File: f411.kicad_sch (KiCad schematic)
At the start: 19 parts, among them J18 Conn_02x04_Top_Bottom, SW1 SW_Push, SW2 SW_Push, U5 STM32F411CEU6

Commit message: completed cleanup of v0.2.0 fixes and switch radio side.
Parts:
- J18: Manufacturer (none) -> Hong Cheng; MfgPart (none) -> HC-PM254-5.0H-2x8PS; Notes (none) -> or equivalent
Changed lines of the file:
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@@
 			)
 		)
+		(property "Note" ""
+			(at 64.77 63.5 0)
+			(effects
+				(font
+					(size 1.27 1.27)
+				)
+				(hide yes)
+			)
+		)
 		(pin "2"
 		)
@@
 			)
 		)
+		(property "Note" ""
+			(at 186.69 152.4 90)
+			(effects
+				(font
+					(size 1.27 1.27)
+				)
+				(hide yes)
+			)
+		)
 		(pin "1"
 		)
@@
 			)
 		)
+		(property "Note" ""
+			(at 167.64 87.63 0)
+			(effects
+				(font
+					(size 1.27 1.27)
+				)
+				(hide yes)
+			)
+		)
 		(pin "1"
 		)
@@
 			)
 		)
+		(property "Note" ""
+			(at 123.19 139.7 0)
+			(effects
+				(font
+					(size 1.27 1.27)
+				)
+				(hide yes)
+			)
+		)
 		(pin "1"
 		)
@@
 			)
 		)
+		(property "Note" ""
+			(at 69.85 85.09 0)
+			(effects
+				(font
+					(size 1.27 1.27)
+				)
+				(hide yes)
+			)
+		)
 		(pin "1"
 		)
@@
 			)
 		)
+		(property "Note" ""
+			(at 106.68 100.33 0)
+			(effects
+				(font
+					(size 1.27 1.27)
+				)
+				(hide yes)
+			)
+		)
 		(pin "1"
 		)
@@
 			)
 		)
+		(property "Note" ""
+			(at 96.52 109.22 0)
+			(effects
+				(font
+					(size 1.27 1.27)
+				)
+				(hide yes)
+			)
+		)
 		(pin "1"
 		)
@@
 			)
 		)
-		(property "Datasheet" "~"
+		(property "Datasheet" "https://www.lcsc.com/datasheet/C42163136.pdf"
 			(at 175.26 128.27 0)
 			(effects
@@
 			)
 		)
+		(property "Manufacturer" "Hong Cheng"
+			(at 175.26 128.27 0)
+			(effects
+				(font
+					(size 1.27 1.27)
+				)
+				(hide yes)
+			)
+		)
+		(property "MfgPart" "HC-PM254-5.0H-2x8PS"
+			(at 175.26 128.27 0)
+			(effects
+				(font
+					(size 1.27 1.27)
+				)
+				(hide yes)
+			)
+		)
+		(property "Note" ""
+			(at 175.26 128.27 0)
+			(effects
+				(font
+					(size 1.27 1.27)
+				)
+				(hide yes)
+			)
+		)
+		(property "Notes" "or equivalent"
+			(at 175.26 128.27 0)
+			(effects
+				(font
+					(size 1.27 1.27)
+				)
+				(hide yes)
+			)
+		)
 		(pin "a1"
 		)
@@
 			)
 		)
+		(property "Note" ""
+			(at 67.31 44.45 90)
+			(effects
+				(font
+					(size 1.27 1.27)
+				)
+				(hide yes)
+			)
+		)
 		(pin "1"
 		)
@@
 			)
 		)
+		(property "Note" ""
+			(at 58.42 59.69 0)
+			(effects
+				(font
+					(size 1.27 1.27)
+				)
+				(hide yes)
+			)
+		)
 		(pin "1"
 		)
@@
 			)
 		)
+		(property "Note" ""
+			(at 170.18 50.8 0)
+			(effects
+				(font
+					(size 1.27 1.27)
+				)
+				(hide yes)
+			)
+		)
 		(pin "1"
 		)
@@
 			)
 		)
+		(property "Note" ""
+			(at 71.12 39.37 0)
+			(effects
+				(font
+					(size 1.27 1.27)
+				)
+				(hide yes)
+			)
+		)
 		(pin "1"
 		)
@@
 			)
 		)
+		(property "Note" ""
+			(at 144.78 102.87 0)
+			(effects
+				(font
+					(size 1.27 1.27)
+				)
+				(hide yes)
+			)
+		)
 		(pin "49"
 		)
@@
 			)
 		)
+		(property "Note" ""
+			(at 170.18 43.18 0)
+			(effects
+				(font
+					(size 1.27 1.27)
+				)
+				(hide yes)
+			)
+		)
 		(pin "2"
 		)
@@
 			)
 		)
+		(property "Note" ""
+			(at 41.91 72.39 90)
+			(effects
+				(font
+					(size 1.27 1.27)
+				)
+				(hide yes)
+			)
+		)
 		(pin "1"
 		)
@@
 			)
 		)
+		(property "Note" ""
+			(at 93.98 40.64 0)
+			(effects
+				(font
+					(size 1.27 1.27)
+				)
+				(hide yes)
+			)
+		)
 		(pin "2"
 		)
@@
 			)
 		)
+		(property "Note" ""
+			(at 190.5 140.97 0)
+			(effects
+				(font
+					(size 1.27 1.27)
+				)
+				(hide yes)
+			)
+		)
 		(pin "1"
 		)
@@
 			)
 		)
+		(property "Note" ""
+			(at 62.23 85.09 90)
+			(effects
+				(font
+					(size 1.27 1.27)
+				)
+				(hide yes)
+			)
+		)
 		(pin "1"
 		)
@@
 			(at 41.91 80.01 0)
 			(effects
+				(font
+					(size 1.27 1.27)
+				)
+				(hide yes)
+			)
+		)
+		(property "Note" ""
+			(at 41.91 80.01 0)
+			(effects

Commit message: converted R, C, and L to smaller 0402 footprints. Some trace rearranging and cleanup.
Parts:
- C14: footprint ProjectLib:C_0603_1608Metric -> ProjectLib:C_0402_1005Metric; Manufacturer Samsung -> (none); MfgPart CL10A475KP8NNNC -> (none); Package C_0603_1608Metric -> C_0402_1005Metric
- C17, C9: footprint ProjectLib:C_0603_1608Metric -> ProjectLib:C_0402_1005Metric; Manufacturer Samsung -> (none); MfgPart CL10B104KB8NNNC -> (none); Package C_0603_1608Metric -> C_0402_1005Metric
- L1: footprint ProjectLib:L_TDK_MLZ1608 -> ProjectLib:L_0402_1005Metric; MfgPart MLZ1608N2R2LT000 -> MLZ1005M2R2WT000; Package L_0603_1608Metric -> L_0402_1005Metric
- R23, R24: footprint ProjectLib:R_0603_1608Metric -> ProjectLib:R_0402_1005Metric; Package R_0603_1608Metric -> R_0402_1005Metric
- R25, R26, R27, R33, R34: footprint ProjectLib:R_0603_1608Metric -> ProjectLib:R_0402_1005Metric; Manufacturer Vishay -> (none); MfgPart CRCW060310K0FKEA -> (none); Package R_0603_1608Metric -> R_0402_1005Metric
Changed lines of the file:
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@@
 			)
 		)
-		(property "Footprint" "ProjectLib:R_0603_1608Metric"
+		(property "Footprint" "ProjectLib:R_0402_1005Metric"
 			(at 62.992 63.5 90)
 			(effects
@@
 			)
 		)
-		(property "Manufacturer" "Vishay"
+		(property "Manufacturer" ""
 			(at 64.77 63.5 0)
 			(effects
@@
 			)
 		)
-		(property "MfgPart" "CRCW060310K0FKEA"
+		(property "MfgPart" ""
 			(at 64.77 63.5 0)
 			(effects
@@
 			)
 		)
-		(property "Package" "R_0603_1608Metric"
+		(property "Package" "R_0402_1005Metric"
 			(at 64.77 63.5 0)
 			(effects
@@
 			)
 		)
-		(property "Footprint" "ProjectLib:R_0603_1608Metric"
+		(property "Footprint" "ProjectLib:R_0402_1005Metric"
 			(at 185.674 152.654 90)
 			(effects
@@
 			)
 		)
-		(property "Manufacturer" "Vishay"
+		(property "Manufacturer" ""
 			(at 186.69 152.4 0)
 			(effects
@@
 			)
 		)
-		(property "MfgPart" "CRCW060310K0FKEA"
+		(property "MfgPart" ""
 			(at 186.69 152.4 0)
 			(effects
@@
 			)
 		)
-		(property "Package" "R_0603_1608Metric"
+		(property "Package" "R_0402_1005Metric"
 			(at 186.69 152.4 0)
 			(effects
@@
 			)
 		)
-		(property "Footprint" "ProjectLib:C_0603_1608Metric"
+		(property "Footprint" "ProjectLib:C_0402_1005Metric"
 			(at 124.1552 143.51 0)
 			(effects
@@
 			)
 		)
-		(property "Manufacturer" "Samsung"
+		(property "Manufacturer" ""
 			(at 123.19 139.7 0)
 			(effects
@@
 			)
 		)
-		(property "MfgPart" "CL10A475KP8NNNC"
+		(property "MfgPart" ""
 			(at 123.19 139.7 0)
 			(effects
@@
 			)
 		)
-		(property "Package" "C_0603_1608Metric"
+		(property "Package" "C_0402_1005Metric"
 			(at 123.19 139.7 0)
 			(effects
@@
 			)
 		)
-		(property "Footprint" "ProjectLib:R_0603_1608Metric"
+		(property "Footprint" "ProjectLib:R_0402_1005Metric"
 			(at 94.742 109.22 90)
 			(effects
@@
 			)
 		)
-		(property "Manufacturer" "Vishay"
+		(property "Manufacturer" ""
 			(at 96.52 109.22 0)
 			(effects
@@
 			)
 		)
-		(property "MfgPart" "CRCW060310K0FKEA"
+		(property "MfgPart" ""
 			(at 96.52 109.22 0)
 			(effects
@@
 			)
 		)
-		(property "Package" "R_0603_1608Metric"
+		(property "Package" "R_0402_1005Metric"
 			(at 96.52 109.22 0)
 			(effects
@@
 			)
 		)
-		(property "Footprint" "ProjectLib:C_0603_1608Metric"
+		(property "Footprint" "ProjectLib:C_0402_1005Metric"
 			(at 71.12 43.4848 0)
 			(effects
@@
 			)
 		)
-		(property "Manufacturer" "Samsung"
+		(property "Manufacturer" ""
 			(at 67.31 44.45 90)
 			(effects
@@
 			)
 		)
-		(property "MfgPart" "CL10B104KB8NNNC"
+		(property "MfgPart" ""
 			(at 67.31 44.45 90)
 			(effects
@@
 			)
 		)
-		(property "Package" "C_0603_1608Metric"
+		(property "Package" "C_0402_1005Metric"
 			(at 67.31 44.45 90)
 			(effects
@@
 			)
 		)
-		(property "Footprint" "ProjectLib:C_0603_1608Metric"
+		(property "Footprint" "ProjectLib:C_0402_1005Metric"
 			(at 171.1452 54.61 0)
 			(effects
@@
 			)
 		)
-		(property "Manufacturer" "Samsung"
+		(property "Manufacturer" ""
 			(at 170.18 50.8 0)
 			(effects
@@
 			)
 		)
-		(property "MfgPart" "CL10B104KB8NNNC"
+		(property "MfgPart" ""
 			(at 170.18 50.8 0)
 			(effects
@@
 			)
 		)
-		(property "Package" "C_0603_1608Metric"
+		(property "Package" "C_0402_1005Metric"
 			(at 170.18 50.8 0)
 			(effects
@@
 			)
 		)
-		(property "Footprint" "ProjectLib:L_TDK_MLZ1608"
+		(property "Footprint" "ProjectLib:L_0402_1005Metric"
 			(at 170.18 43.18 0)
 			(effects
@@
 			)
 		)
-		(property "Datasheet" "https://product.tdk.com/en/system/files?file=dam/doc/product/inductor/inductor/smd/catalog/inductor_commercial_decoupling_mlz1608_en.pdf"
+		(property "Datasheet" "https://product.tdk.com/en/system/files?file=dam/doc/product/inductor/inductor/smd/catalog/inductor_commercial_decoupling_mlz1005_en.pdf"
 			(at 170.18 43.18 0)
 			(effects
@@
 			)
 		)
-		(property "MfgPart" "MLZ1608N2R2LT000"
+		(property "MfgPart" " MLZ1005M2R2WT000"
 			(at 170.18 43.18 0)
 			(effects
@@
 			)
 		)
-		(property "Package" "L_0603_1608Metric"
+		(property "Package" "L_0402_1005Metric"
 			(at 170.18 43.18 0)
 			(effects
@@
 			)
 		)
-		(property "Footprint" "ProjectLib:R_0603_1608Metric"
+		(property "Footprint" "ProjectLib:R_0402_1005Metric"
 			(at 92.202 40.64 90)
 			(effects
@@
 			)
 		)
-		(property "Manufacturer" "Vishay"
+		(property "Manufacturer" ""
 			(at 93.98 40.64 0)
 			(effects
@@
 			)
 		)
-		(property "MfgPart" "CRCW060310K0FKEA"
+		(property "MfgPart" ""
 			(at 93.98 40.64 0)
 			(effects
@@
 			)
 		)
-		(property "Package" "R_0603_1608Metric"
+		(property "Package" "R_0402_1005Metric"
 			(at 93.98 40.64 0)
 			(effects
@@
 			)
 		)
-		(property "Footprint" "ProjectLib:R_0603_1608Metric"
+		(property "Footprint" "ProjectLib:R_0402_1005Metric"
 			(at 189.484 141.224 90)
 			(effects
@@
 			)
 		)
-		(property "Manufacturer" "Vishay"
+		(property "Manufacturer" ""
 			(at 190.5 140.97 0)
 			(effects
@@
 			)
 		)
-		(property "MfgPart" "CRCW060310K0FKEA"
+		(property "MfgPart" ""
 			(at 190.5 140.97 0)
 			(effects
@@
 			)
 		)
-		(property "Package" "R_0603_1608Metric"
+		(property "Package" "R_0402_1005Metric"
 			(at 190.5 140.97 0)
 			(effects
@@
 			)
 		)
-		(property "Footprint" "ProjectLib:R_0603_1608Metric"
+		(property "Footprint" "ProjectLib:R_0402_1005Metric"
 			(at 62.23 86.868 90)
 			(effects
@@
 			)
 		)
-		(property "Package" "R_0603_1608Metric"
+		(property "Package" "R_0402_1005Metric"
 			(at 62.23 85.09 90)
 			(effects
@@
 			)
 		)
-		(property "Footprint" "ProjectLib:R_0603_1608Metric"
+		(property "Footprint" "ProjectLib:R_0402_1005Metric"
 			(at 40.132 80.01 90)
 			(effects
@@
 			)
 		)
-		(property "Package" "R_0603_1608Metric"
+		(property "Package" "R_0402_1005Metric"
 			(at 41.91 80.01 0)
 			(effects

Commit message: some (documentation) cleanup while submitting for fabrication.
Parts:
- J18: MountType (none) -> SMT; Package (none) -> 2x04_P2.54mm, verticle pinsocket
- TP1: MountType (none) -> SMT
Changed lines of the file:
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@@
 			)
 		)
-		(property "Datasheet" ""
+		(property "Datasheet" "https://www.kingbrightusa.com/images/catalog/SPEC/APT1608LVBC-D.pdf"
 			(at 69.85 85.09 0)
 			(effects
@@
 			)
 		)
+		(property "MountType" "SMT"
+			(at 106.68 100.33 0)
+			(effects
+				(font
+					(size 1.27 1.27)
+				)
+				(hide yes)
+			)
+		)
 		(pin "1"
 		)
@@
 			)
 		)
-		(property "Description" "Generic connector, double row, 02x04, row letter first pin numbering scheme (pin number consists of a letter for the row and a number for the pin index in this row. a1, ..., aN; b1, ..., bN), script generated (kicad-library-utils/schlib/autogen/connector/)"
+		(property "Description" "PinSocket  02x04 connector, low profile"
 			(at 175.26 128.27 0)
 			(effects
@@
 		)
 		(property "Notes" "or equivalent"
+			(at 175.26 128.27 0)
+			(effects
+				(font
+					(size 1.27 1.27)
+				)
+				(hide yes)
+			)
+		)
+		(property "MountType" "SMT"
+			(at 175.26 128.27 0)
+			(effects
+				(font
+					(size 1.27 1.27)
+				)
+				(hide yes)
+			)
+		)
+		(property "Package" "2x04_P2.54mm, verticle pinsocket"
 			(at 175.26 128.27 0)
 			(effects
@@
 			)
 		)
-		(property "Datasheet" ""
+		(property "Datasheet" "https://www.kingbrightusa.com/images/catalog/SPEC/APT1608LSECK-J3-PRV.pdf"
 			(at 41.91 72.39 0)
 			(effects

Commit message: v0.2.2 with BOM fixes, some additional documentation and cleanup.
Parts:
- J18: MfgPart HC-PM254-5.0H-2x8PS -> HC-PM254-5.0H-2x4PS-02A
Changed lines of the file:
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@@
 			)
 		)
-		(property "Datasheet" "https://www.lcsc.com/datasheet/C42163136.pdf"
+		(property "Datasheet" "https://www.lcsc.com/product-detail/C42163132.html"
 			(at 175.26 128.27 0)
 			(effects
@@
 			)
 		)
-		(property "MfgPart" "HC-PM254-5.0H-2x8PS"
+		(property "MfgPart" "HC-PM254-5.0H-2x4PS-02A"
 			(at 175.26 128.27 0)
 			(effects

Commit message: improved schematic sheet titles.
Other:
- title: ADCs for 10K thermistors -> stm32f411, ST-Link & SSD
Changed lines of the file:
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@@
 	(paper "A4")
 	(title_block
-		(title "ADCs for 10K thermistors")
-		(date "2025-01-07")
-		(rev "v0.1.1")
+		(title "stm32f411, ST-Link & SSD")
+		(date "2025-09-15")
+		(rev "v0.2.2")
 	)
 	(text "SSD"

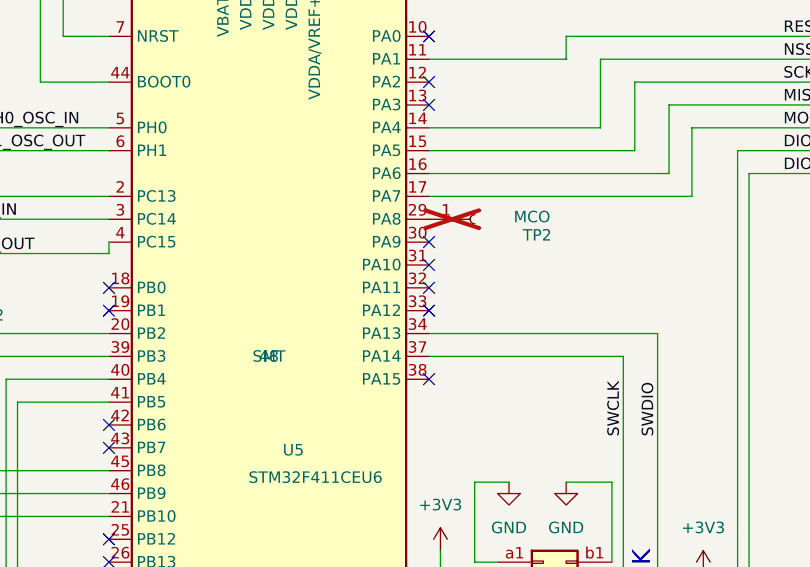
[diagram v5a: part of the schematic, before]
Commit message: added new battery holder footprint.
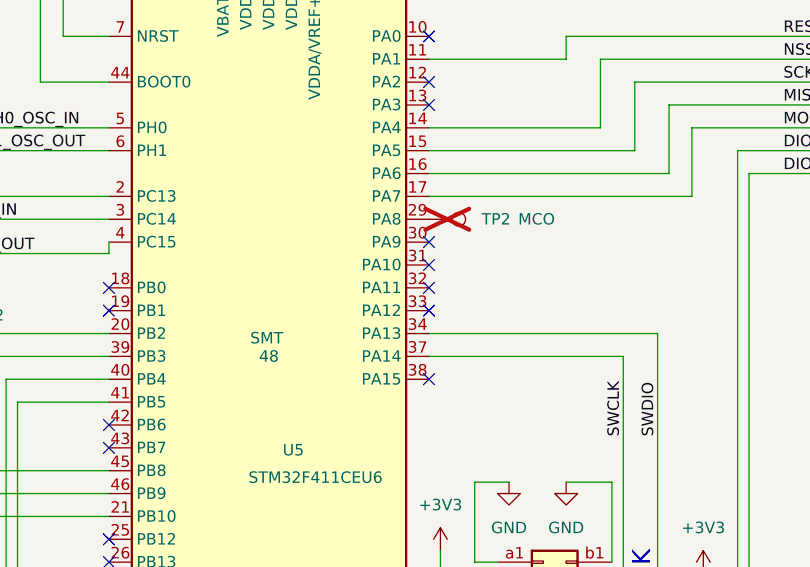
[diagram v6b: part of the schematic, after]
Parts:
- TP2: symbol ProjectLib:Conn_01x01_Socket -> ProjectLib:TestPoint; MountType PTH -> SMT; now in the parts list
- U5: footprint ProjectLib:QFN-48-1EP_7x7mm_P0.5mm_EP5.6x5.6mm -> Package_DFN_QFN:QFN-48-1EP_7x7mm_P0.5mm_EP5.6x5.6mm

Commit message: added gnd-radio and gnd-ant zones on two layers. ERC and DRC mostly good. (Two warnings about pads field in NetTie footprints.)
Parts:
- U5: footprint Package_DFN_QFN:QFN-48-1EP_7x7mm_P0.5mm_EP5.6x5.6mm -> ProjectLib:QFN-48-1EP_7x7mm_P0.5mm_EP5.6x5.6mm
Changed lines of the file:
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@@
 			)
 		)
-		(property "Footprint" "Package_DFN_QFN:QFN-48-1EP_7x7mm_P0.5mm_EP5.6x5.6mm"
+		(property "Footprint" "ProjectLib:QFN-48-1EP_7x7mm_P0.5mm_EP5.6x5.6mm"
 			(at 129.54 140.97 0)
 			(hide yes)

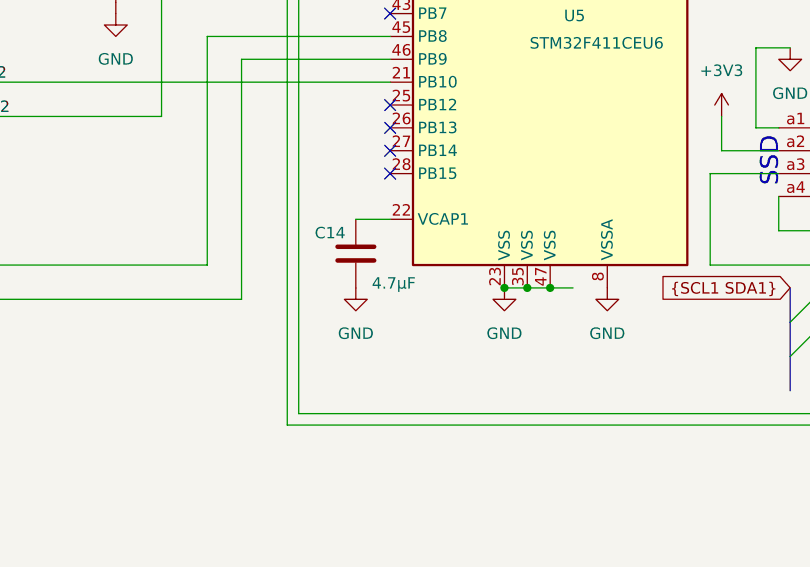
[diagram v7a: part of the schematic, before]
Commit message: added QR and ID blocks on silkscreen. Marked HSE and LSE as DNP. Revised version number to 0.3.1.
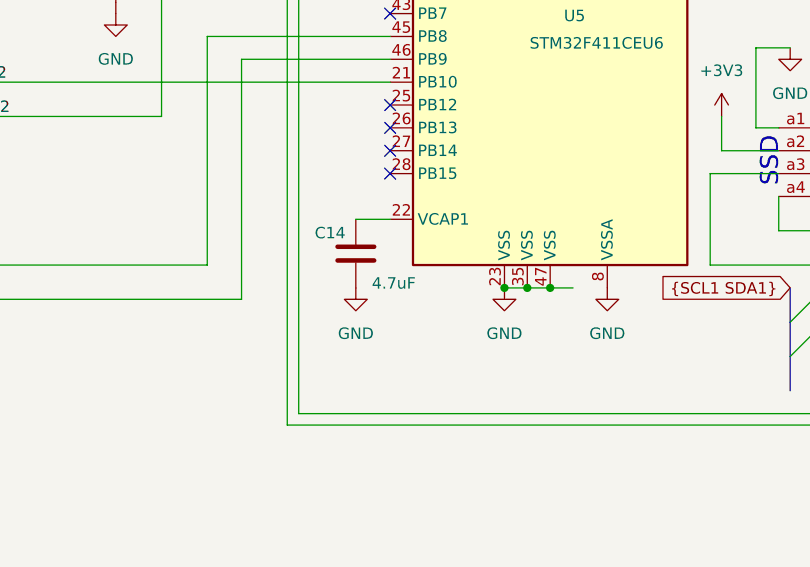
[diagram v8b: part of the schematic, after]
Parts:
- C14: value 4.7µF -> 4.7uF
- TP1, TP2: Package (none) -> none; now left out of the parts list
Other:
- title: stm32f411, ST-Link & SSD -> stm32f411, RFM95W
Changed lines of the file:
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@@
 	(paper "A4")
 	(title_block
-		(title "stm32f411, ST-Link & SSD")
-		(date "2025-09-15")
-		(rev "v0.2.2")
+		(title "stm32f411, RFM95W")
+		(date "2026-04-12")
+		(rev "v0.3.1")
 	)
 	(text "SSD"
@@
 		(body_style 1)
 		(exclude_from_sim no)
-		(in_bom yes)
+		(in_bom no)
 		(on_board yes)
-		(in_pos_files yes)
+		(in_pos_files no)
 		(dnp yes)
 		(property "Reference" "TP2"
@@
 			)
 		)
-		(property "Package" ""
+		(property "Package" "none"
 			(at 162.56 87.63 0)
 			(hide yes)
@@
 			)
 		)
-		(property "Value" "4.7µF"
+		(property "Value" "4.7uF"
 			(at 124.968 143.002 0)
 			(show_name no)
@@
 		(body_style 1)
 		(exclude_from_sim no)
-		(in_bom yes)
+		(in_bom no)
 		(on_board yes)
-		(in_pos_files yes)
+		(in_pos_files no)
 		(dnp yes)
 		(fields_autoplaced yes)
@@
 			(at 106.68 100.33 0)
 			(hide yes)
+			(show_name no)
+			(do_not_autoplace no)
+			(effects
+				(font
+					(size 1.27 1.27)
+				)
+			)
+		)
+		(property "Package" "none"
+			(at 106.68 100.33 0)
+			(hide yes)
